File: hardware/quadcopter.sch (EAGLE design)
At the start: 62 parts, among them J1 AVR_SPI_PRG_6NS, J2 HEADER-4POS-2X2-0.1IN-FEMALE-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, J3 HEADER-10POSTH-254X10, J4 HEADER-4POS-0.1IN-FEMALE-SMD-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, Q1 MOSFET-SI2302CDS-T1-E3CT-ND, Q2 MOSFET-SI2302CDS-T1-E3CT-ND, Q3 MOSFET-SI2302CDS-T1-E3CT-ND, Q4 MOSFET-SI2302CDS-T1-E3CT-ND, Q5 MOSFET-SI2302CDS-T1-E3CT-ND, Q6 MOSFET-SI2302CDS-T1-E3CT-ND, SW1 PUSHBUTTON_SMD-VERTICAL-1, U1 ATMEGA128RFA1, U2 LSM-IMU-497-18367-1-NDIMU, Y1 CRYSTAL5X3

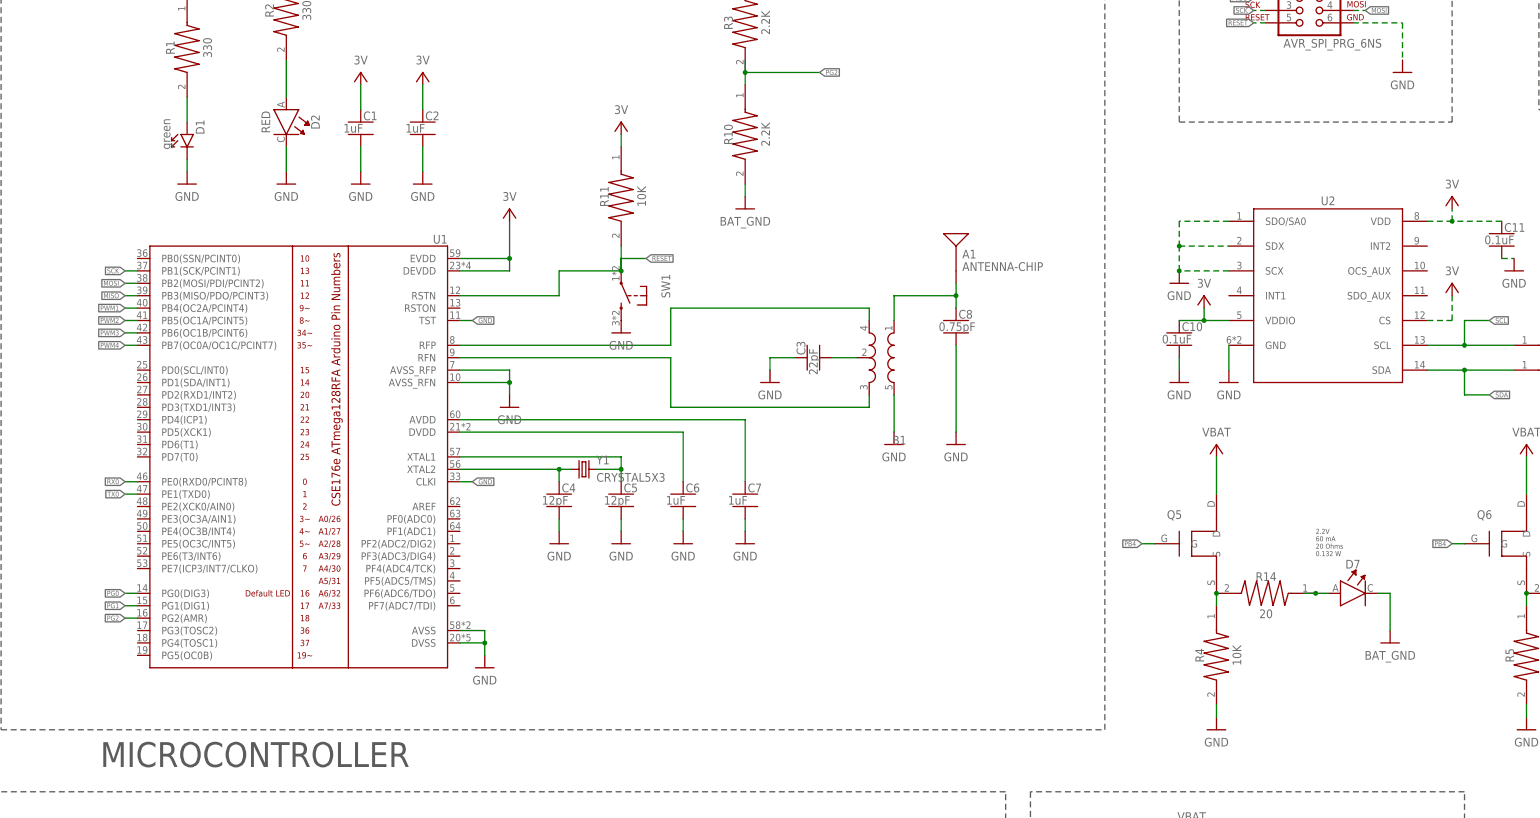
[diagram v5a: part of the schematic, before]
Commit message: changed actual library name
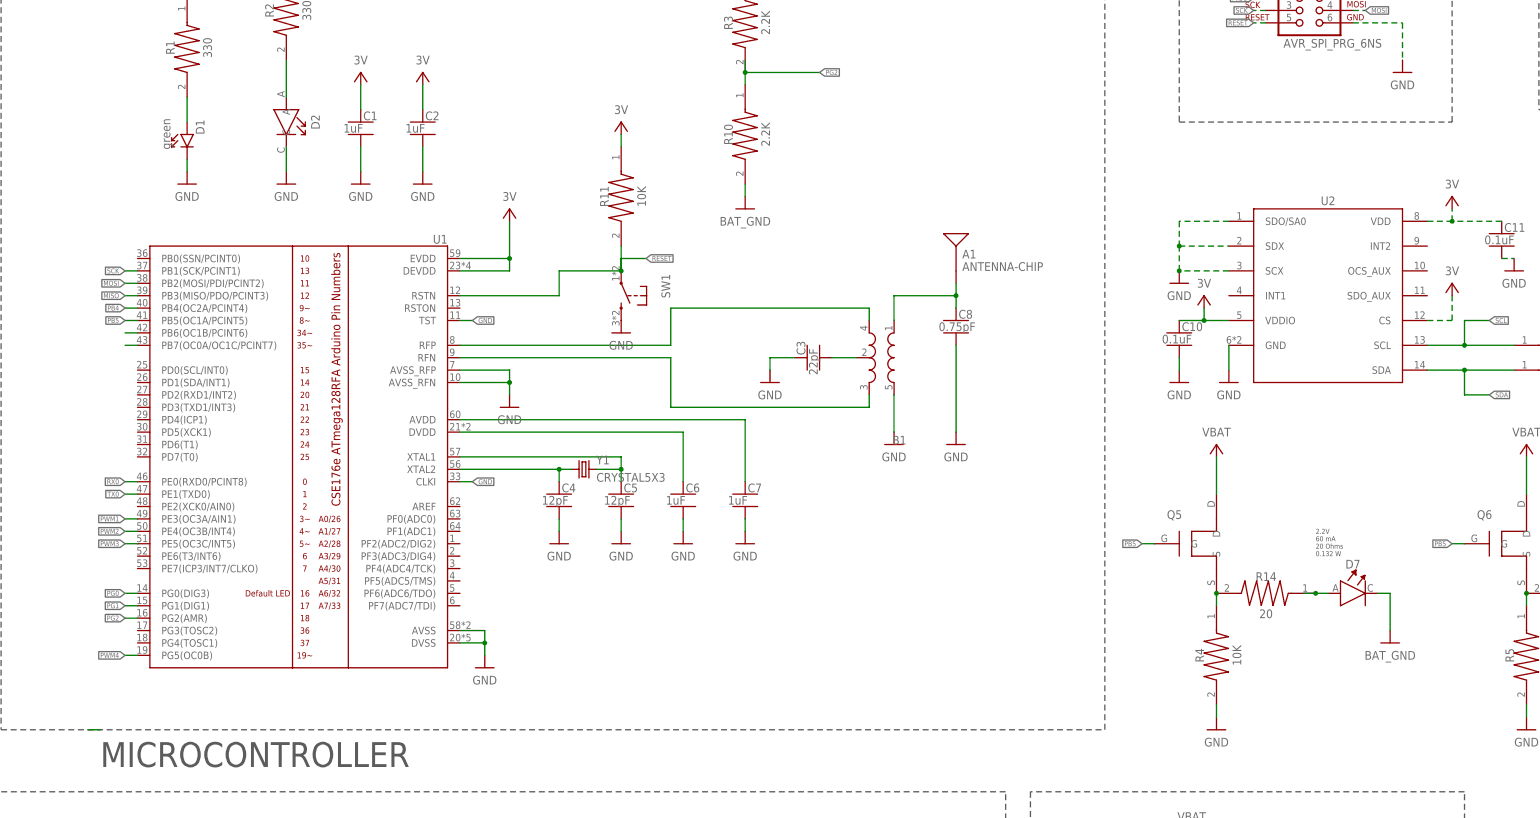
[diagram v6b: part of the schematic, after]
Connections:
- new net N$24: U1.PB6(OC1B/PCINT6)
- new net N$25: U1.PB7(OC0A/OC1C/PCINT7)
- new net PB5: Q5.G, Q6.G, U1.PB5(OC1A/PCINT5)
- net PB4: now also U1.PB4(OC2A/PCINT4); no longer Q5.G, Q6.G
- net PWM1: now also U1.PE3(OC3A/AIN1); no longer U1.PB4(OC2A/PCINT4)
- net PWM2: now also U1.PE4(OC3B/INT4); no longer U1.PB5(OC1A/PCINT5)
- net PWM3: now also U1.PE5(OC3C/INT5); no longer U1.PB6(OC1B/PCINT6)
- net PWM4: now also U1.PG5(OC0B); no longer U1.PB7(OC0A/OC1C/PCINT7)
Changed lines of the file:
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@@
 <instance part="D2" gate="G$1" x="48.26" y="193.04" smashed="yes" rot="R270">
 <attribute name="NAME" x="53.34" y="193.04" size="1.778" layer="95" rot="R270" align="bottom-center"/>
-<attribute name="VALUE" x="43.18" y="193.04" size="1.778" layer="96" rot="R270" align="bottom-center"/>
 </instance>
 <instance part="P+1" gate="G$1" x="63.5" y="203.2" smashed="yes">
@@
 <segment>
 <wire x1="48.26" y1="205.74" x2="48.26" y2="198.12" width="0.1524" layer="91"/>
+<pinref part="R2" gate="G$1" pin="2"/>
 <pinref part="D2" gate="G$1" pin="A"/>
-<pinref part="R2" gate="G$1" pin="2"/>
 </segment>
 </net>
@@
 <wire x1="116.84" y1="165.1" x2="121.92" y2="165.1" width="0.1524" layer="91"/>
 <junction x="116.84" y="162.56"/>
+<pinref part="R11" gate="G$1" pin="2"/>
 <pinref part="SW1" gate="G$1" pin="1"/>
-<pinref part="R11" gate="G$1" pin="2"/>
 </segment>
 <segment>
@@
 </segment>
 <segment>
-<pinref part="U1" gate="G$1" pin="PB5(OC1A/PCINT5)"/>
-<wire x1="17.78" y1="152.4" x2="15.24" y2="152.4" width="0.1524" layer="91"/>
-<label x="15.24" y="152.4" size="1.016" layer="95" rot="R180" xref="yes"/>
-</segment>
-<segment>
 <wire x1="340.36" y1="172.72" x2="345.44" y2="172.72" width="0.1524" layer="91"/>
 <label x="345.44" y="172.72" size="1.016" layer="95" xref="yes"/>
 <pinref part="J3" gate="G$1" pin="7"/>
+</segment>
+<segment>
+<wire x1="17.78" y1="109.22" x2="15.24" y2="109.22" width="0.1524" layer="91"/>
+<label x="15.24" y="109.22" size="1.016" layer="95" rot="R180" xref="yes"/>
+<pinref part="U1" gate="G$1" pin="PE4(OC3B/INT4)"/>
 </segment>
 </net>
@@
 </segment>
 <segment>
-<pinref part="U1" gate="G$1" pin="PB4(OC2A/PCINT4)"/>
-<wire x1="17.78" y1="154.94" x2="15.24" y2="154.94" width="0.1524" layer="91"/>
-<label x="15.24" y="154.94" size="1.016" layer="95" rot="R180" xref="yes"/>
-</segment>
-<segment>
 <wire x1="340.36" y1="177.8" x2="345.44" y2="177.8" width="0.1524" layer="91"/>
 <label x="345.44" y="177.8" size="1.016" layer="95" xref="yes"/>
 <pinref part="J3" gate="G$1" pin="9"/>
+</segment>
+<segment>
+<pinref part="U1" gate="G$1" pin="PE3(OC3A/AIN1)"/>
+<wire x1="17.78" y1="111.76" x2="15.24" y2="111.76" width="0.1524" layer="91"/>
+<label x="15.24" y="111.76" size="1.016" layer="95" rot="R180" xref="yes"/>
 </segment>
 </net>
@@
 </segment>
 <segment>
-<pinref part="U1" gate="G$1" pin="PB6(OC1B/PCINT6)"/>
-<wire x1="17.78" y1="149.86" x2="15.24" y2="149.86" width="0.1524" layer="91"/>
-<label x="15.24" y="149.86" size="1.016" layer="95" rot="R180" xref="yes"/>
-</segment>
-<segment>
 <wire x1="340.36" y1="170.18" x2="345.44" y2="170.18" width="0.1524" layer="91"/>
 <label x="345.44" y="170.18" size="1.016" layer="95" xref="yes"/>
 <pinref part="J3" gate="G$1" pin="6"/>
+</segment>
+<segment>
+<wire x1="17.78" y1="106.68" x2="15.24" y2="106.68" width="0.1524" layer="91"/>
+<label x="15.24" y="106.68" size="1.016" layer="95" rot="R180" xref="yes"/>
+<pinref part="U1" gate="G$1" pin="PE5(OC3C/INT5)"/>
 </segment>
 </net>
@@
 </segment>
 <segment>
-<pinref part="U1" gate="G$1" pin="PB7(OC0A/OC1C/PCINT7)"/>
-<wire x1="17.78" y1="147.32" x2="15.24" y2="147.32" width="0.1524" layer="91"/>
-<label x="15.24" y="147.32" size="1.016" layer="95" rot="R180" xref="yes"/>
-</segment>
-<segment>
 <wire x1="340.36" y1="167.64" x2="345.44" y2="167.64" width="0.1524" layer="91"/>
 <label x="345.44" y="167.64" size="1.016" layer="95" xref="yes"/>
 <pinref part="J3" gate="G$1" pin="5"/>
+</segment>
+<segment>
+<wire x1="17.78" y1="83.82" x2="15.24" y2="83.82" width="0.1524" layer="91"/>
+<label x="15.24" y="83.82" size="1.016" layer="95" rot="R180" xref="yes"/>
+<pinref part="U1" gate="G$1" pin="PG5(OC0B)"/>
 </segment>
 </net>
@@
 </segment>
 </net>
-<net name="PB4" class="0">
+<net name="PB5" class="0">
 <segment>
 <pinref part="Q5" gate="G$1" pin="G"/>
@@
 <wire x1="289.56" y1="106.68" x2="287.02" y2="106.68" width="0.1524" layer="91"/>
 <label x="287.02" y="106.68" size="1.016" layer="95" rot="R180" xref="yes"/>
+</segment>
+<segment>
+<pinref part="U1" gate="G$1" pin="PB5(OC1A/PCINT5)"/>
+<wire x1="17.78" y1="152.4" x2="15.24" y2="152.4" width="0.1524" layer="91"/>
+<label x="15.24" y="152.4" size="1.016" layer="95" rot="R180" xref="yes"/>
 </segment>
 </net>
@@
 </segment>
 </net>
+<net name="PWM5" class="0">
+<segment>
+<wire x1="10.16" y1="68.58" x2="7.62" y2="68.58" width="0.1524" layer="91"/>
+</segment>
+</net>
+<net name="N$24" class="0">
+<segment>
+<pinref part="U1" gate="G$1" pin="PB6(OC1B/PCINT6)"/>
+<wire x1="17.78" y1="149.86" x2="15.24" y2="149.86" width="0.1524" layer="91"/>
+</segment>
+</net>
+<net name="N$25" class="0">
+<segment>
+<pinref part="U1" gate="G$1" pin="PB7(OC0A/OC1C/PCINT7)"/>
+<wire x1="17.78" y1="147.32" x2="15.24" y2="147.32" width="0.1524" layer="91"/>
+</segment>
+</net>
+<net name="PB4" class="0">
+<segment>
+<pinref part="U1" gate="G$1" pin="PB4(OC2A/PCINT4)"/>
+<wire x1="17.78" y1="154.94" x2="15.24" y2="154.94" width="0.1524" layer="91"/>
+<label x="15.24" y="154.94" size="1.016" layer="95" rot="R180" xref="yes"/>
+</segment>
+</net>

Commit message: actually made the library name changes for real this time
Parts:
- NET-BRIDGE: device custom.lbr:NET-BRIDGE -> custom_.lbr:NET-BRIDGE
- Q1, Q2, Q3, Q4, Q5, Q6: device custom.lbr:MOSFET-SI2302CDS-T1-E3CT-ND -> custom_.lbr:MOSFET-SI2302CDS-T1-E3CT-ND
- R1, R2: device custom.lbr:MY-RESISTOR-0805330OHMRES -> custom_.lbr:MY-RESISTOR-0805330OHMRES
- R10, R3: device custom.lbr:MY-RESISTOR-08052.2KOHMRES -> custom_.lbr:MY-RESISTOR-08052.2KOHMRES
- R11, R12, R13, R4, R5, R6, R7, R8, R9: device custom.lbr:MY-RESISTOR-080510KOHMRES -> custom_.lbr:MY-RESISTOR-080510KOHMRES
- R14, R15: device custom.lbr:MY-RESISTOR-080520OHMRES -> custom_.lbr:MY-RESISTOR-080520OHMRES
- U2: device custom.lbr:LSM-IMU-497-18367-1-NDIMU -> custom_.lbr:LSM-IMU-497-18367-1-NDIMU

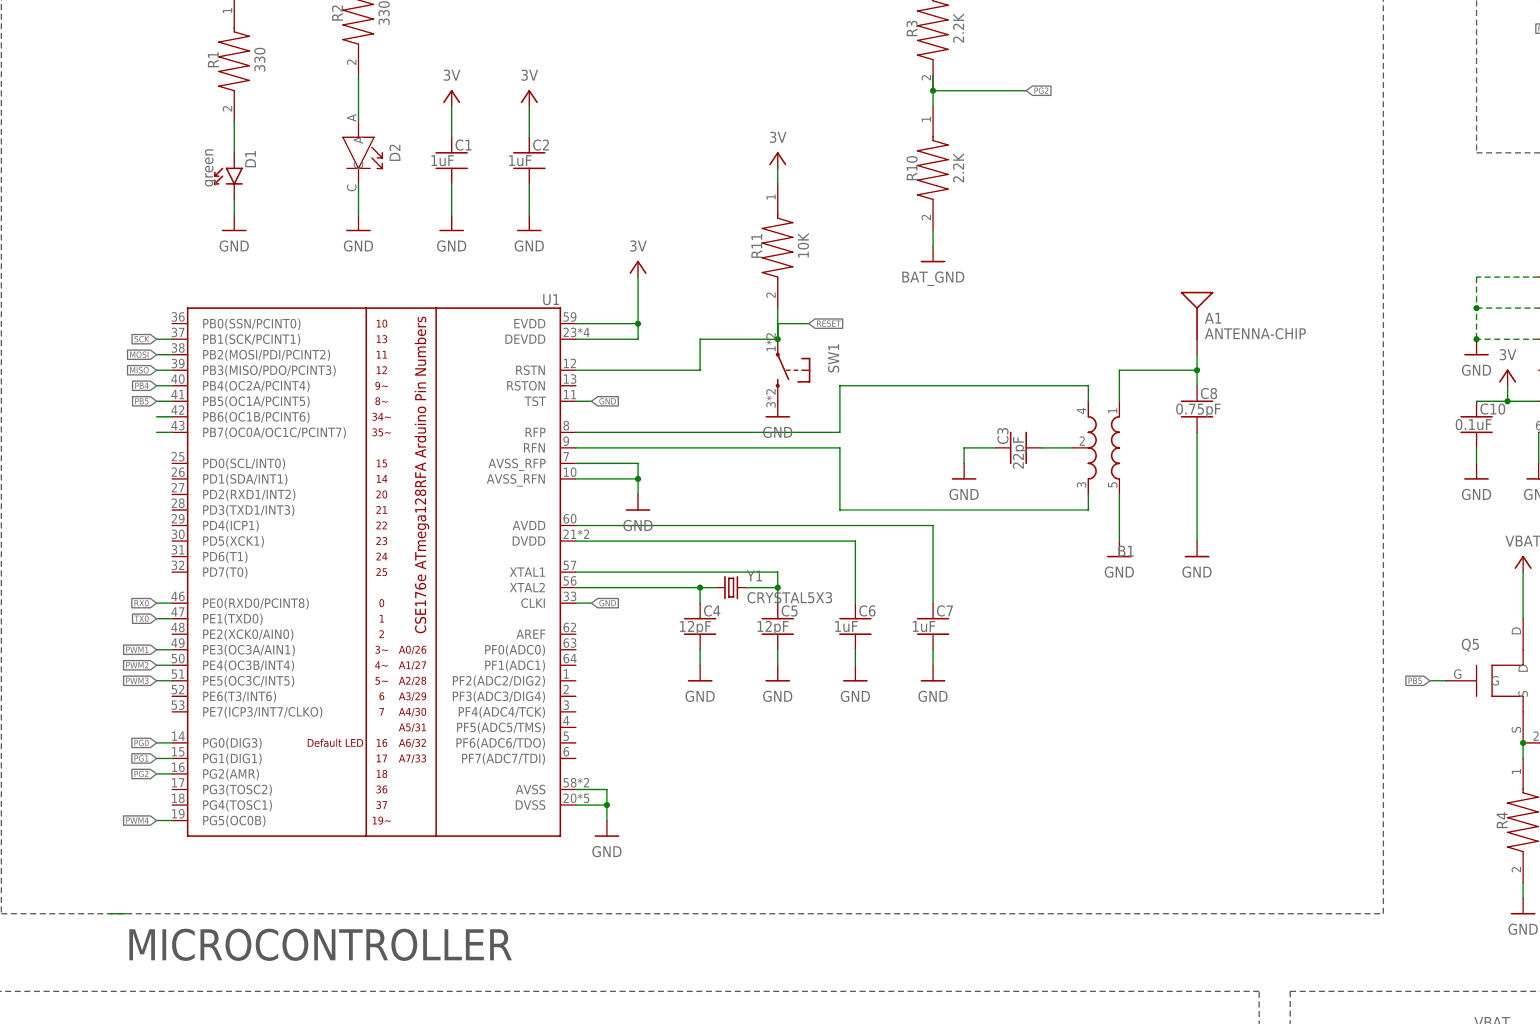
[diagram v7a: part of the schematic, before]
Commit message: got rid of library
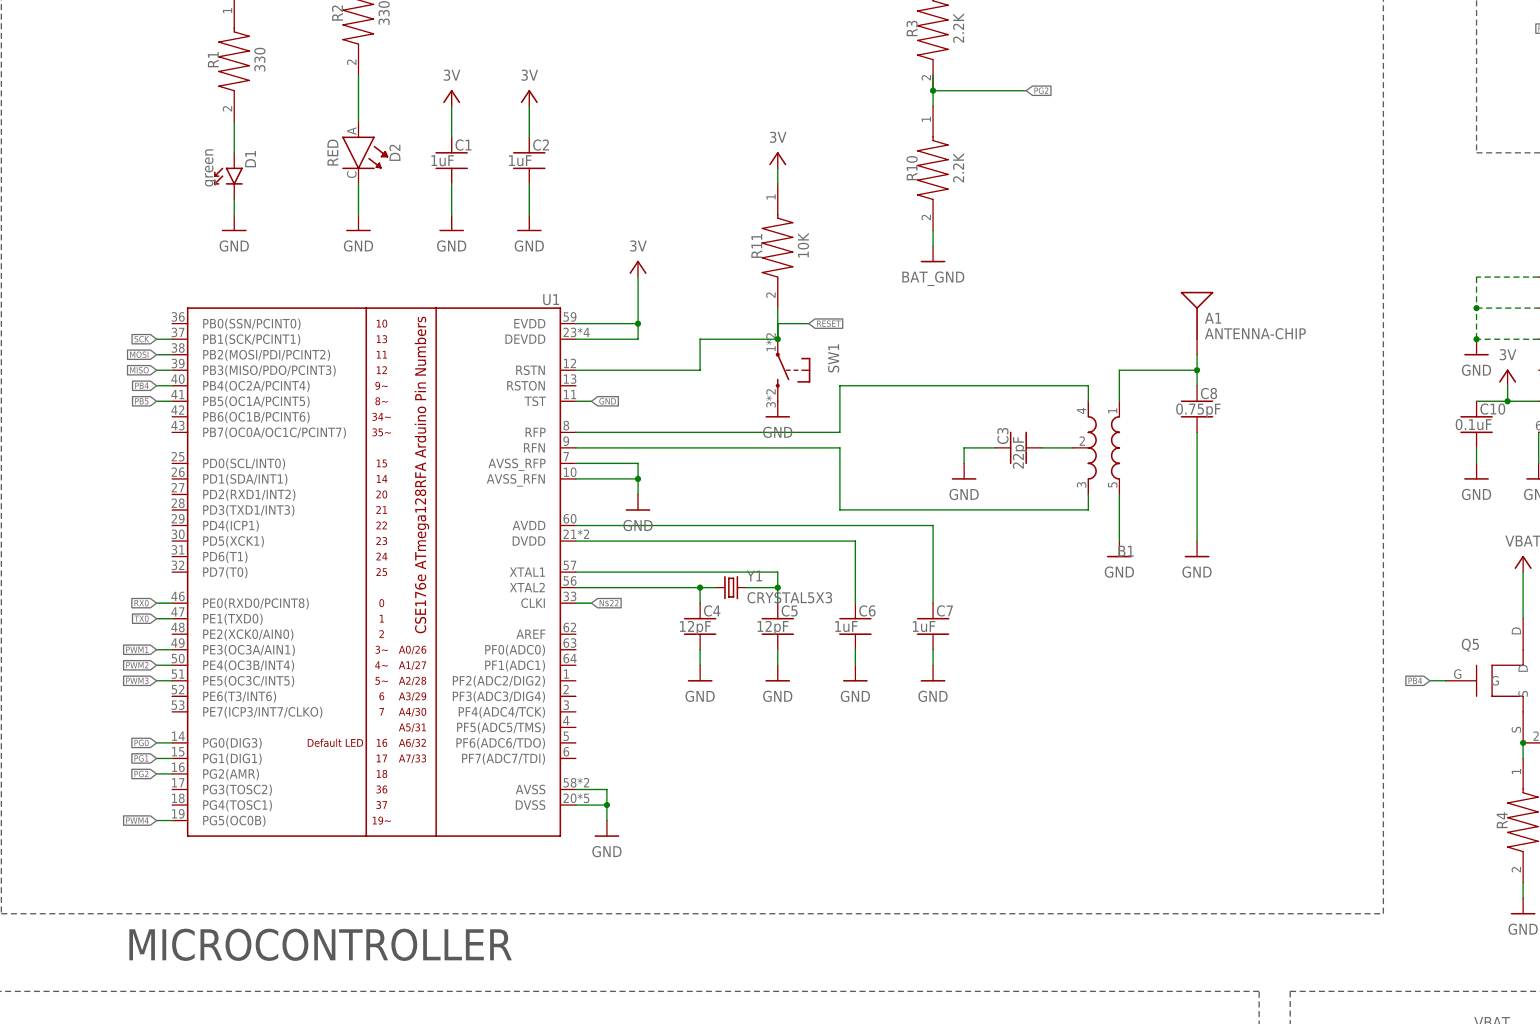
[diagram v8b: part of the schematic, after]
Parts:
- D1: device quadparts_prebuilt:DIODE-LED_SMD-2012-0805-GREEN -> quadparts_prebuilt_2022:DIODE-LED_SMD-2012-0805-GREEN
- D2: device custom:LED-RED-LED -> custom_.lbr:LED-RED-LED
- U1: device quadparts_prebuilt:ATMEGA128RFA1 -> quadparts_prebuilt_2022:ATMEGA128RFA1
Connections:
- removed net N$24: U1.PB6(OC1B/PCINT6)
- removed net N$25: U1.PB7(OC0A/OC1C/PCINT7)
- new net N$22: U1.CLKI
- net GND: no longer U1.CLKI
- net PB4: now also Q5.G
- net PB5: no longer Q5.G
